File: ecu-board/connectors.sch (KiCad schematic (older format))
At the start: 34 parts, among them J10 Injector connector, J11 Cockpit connector, J12 EGO connector, J13 Chrankshaft Hall connector, J14 Camshaft Hall connector, J15 Ignition 1 connector, J16 Ignition 2 connector, J17 Camera connector, J18 Wheel Hall connector, J2 Battery power conenctor, J4 Motor connector, J5 Serial DB9 connector, J6 Controller connector, J7 Backlight connector, J8 IAT connector, J9 CLT connector

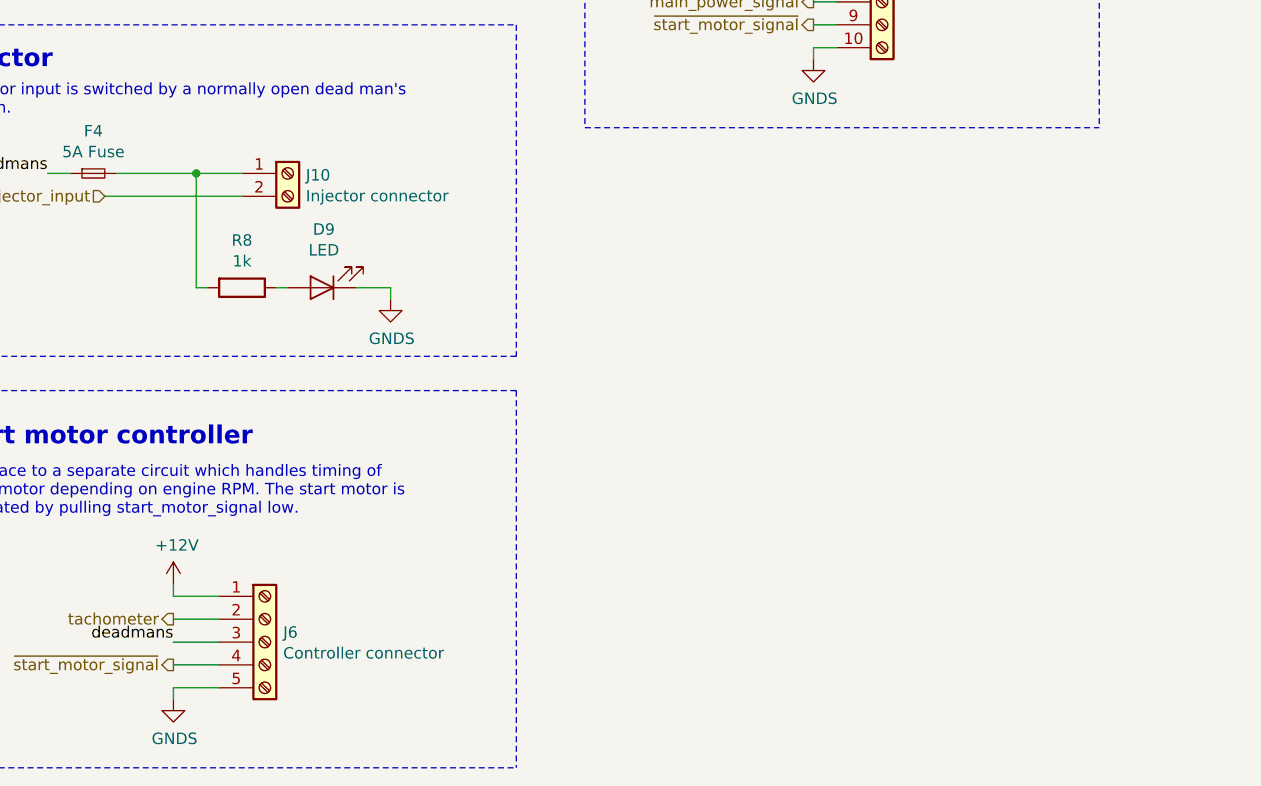
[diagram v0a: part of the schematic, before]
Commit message: Add CAN connector.
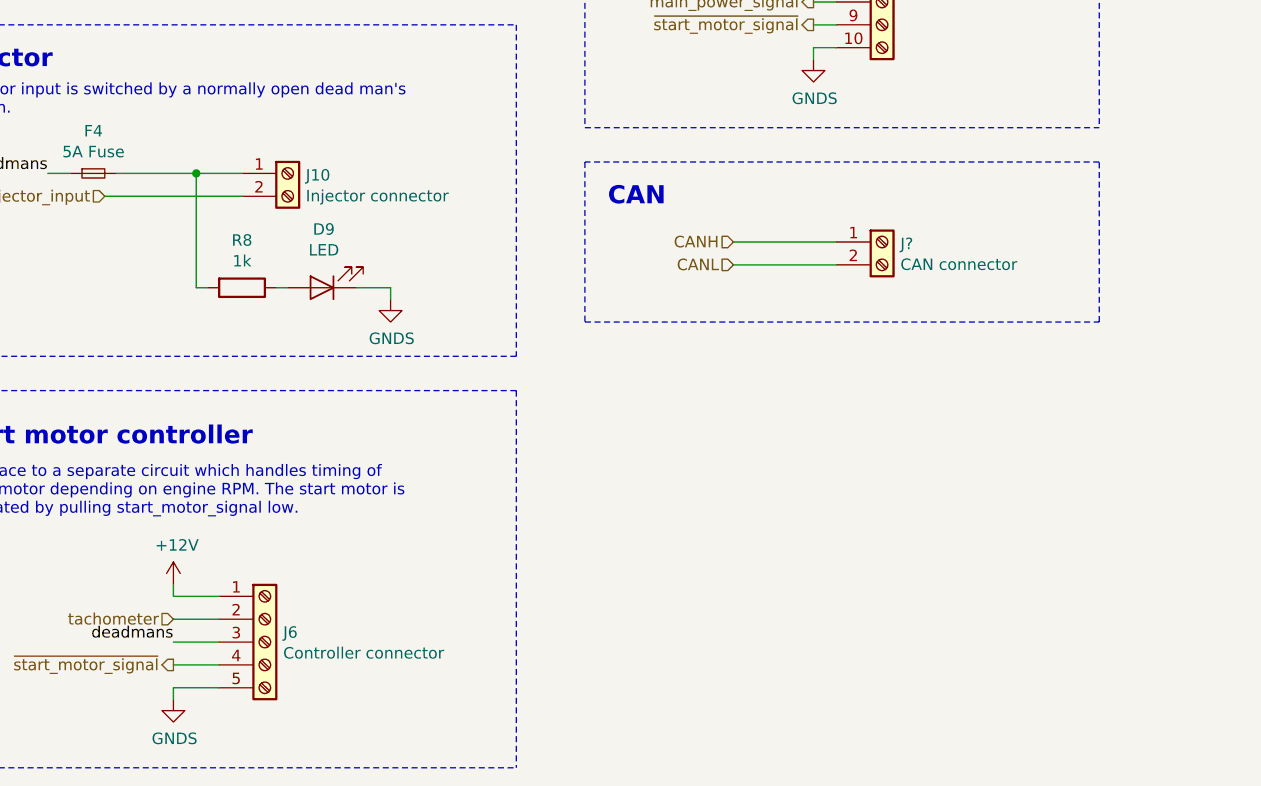
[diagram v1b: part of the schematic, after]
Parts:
- added J?: CAN connector, ecu-board-footprints:Terminal_Block_2x5.00mm, symbol Connector:Screw_Terminal_01x02
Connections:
- new net CANH: J?.1 (Pin_1)
- new net CANL: J?.2 (Pin_2)
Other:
- note added: "CAN"
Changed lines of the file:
@@
 	1    0    0    -1
 $EndComp
-Text HLabel 1900 9050 0    50   Output ~ 0
+Text HLabel 1900 9050 0    50   Input ~ 0
 tachometer
 Wire Wire Line
@@
 Wire Wire Line
 	1700 2300 2100 2300
+$Comp
+L Connector:Screw_Terminal_01x02 J?
+U 1 1 5D94B35C
+P 5000 7400
+F 0 "J?" H 5080 7392 50  0000 L CNN
+F 1 "CAN connector" H 5080 7301 50  0000 L CNN
+F 2 "ecu-board-footprints:Terminal_Block_2x5.00mm" H 5000 7400 50  0001 C CNN
+F 3 "~" H 5000 7400 50  0001 C CNN
+F 4 "Würth" H 5000 7400 50  0001 C CNN "Manufacturer"
+F 5 "2141 Series" H 5000 7400 50  0001 C CNN "Part no."
+	1    5000 7400
+	1    0    0    -1
+$EndComp
+Text Notes 3800 7250 0    79   ~ 16
+CAN
+Text HLabel 4350 7400 0    50   Input ~ 0
+CANH
+Text HLabel 4350 7500 0    50   Input ~ 0
+CANL
+Wire Wire Line
+	4350 7500 4800 7500
+Wire Wire Line
+	4800 7400 4350 7400
+Wire Notes Line
+	3700 7050 3700 7750
+Wire Notes Line
+	3700 7750 5950 7750
+Wire Notes Line
+	5950 7750 5950 7050
+Wire Notes Line
+	5950 7050 3700 7050
 $EndSCHEMATC

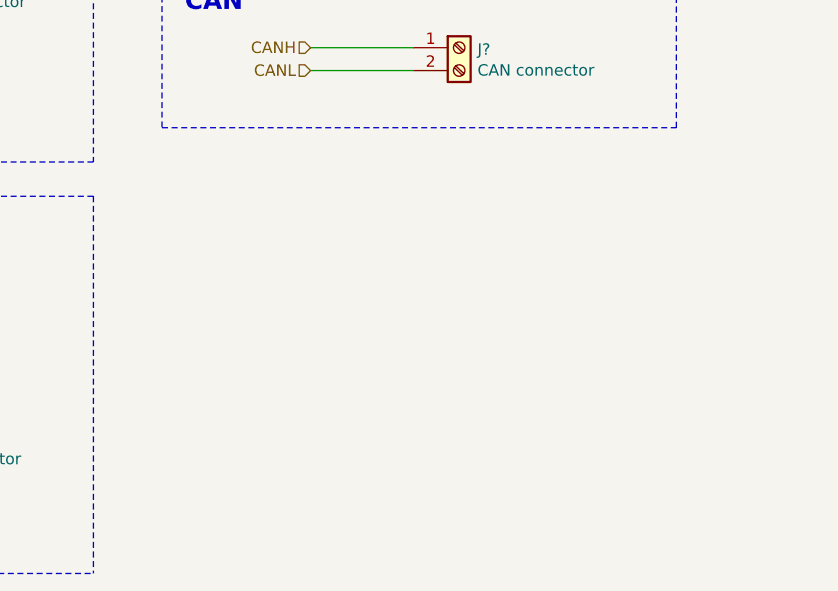
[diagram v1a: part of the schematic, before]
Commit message: Add speed sensor connector.
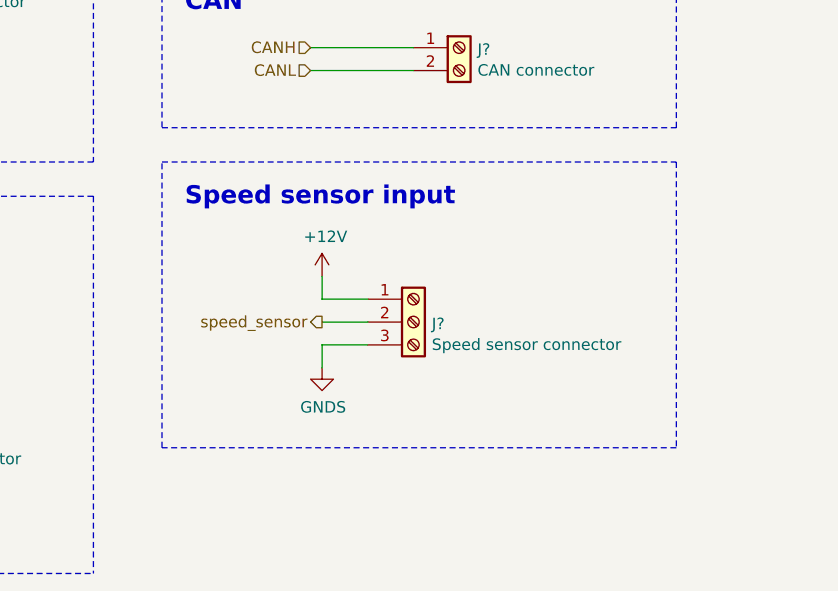
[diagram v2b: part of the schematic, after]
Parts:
- added J?: Speed sensor connector, ecu-board-footprints:Terminal_Block_3x5.00mm, symbol Connector:Screw_Terminal_01x03
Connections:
- net +12V: now also J?.1 (Pin_1)
- net GNDS: now also J?.3 (Pin_3)
- new net speed_sensor: J?.2 (Pin_2)
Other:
- note added: "Speed sensor input"
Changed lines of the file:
@@
 Wire Notes Line
 	5950 7050 3700 7050
+Text Notes 3800 8100 0    79   ~ 16
+Speed sensor input
+$Comp
+L Connector:Screw_Terminal_01x03 J?
+U 1 1 5DA598D9
+P 4800 8600
+F 0 "J?" H 4880 8592 50  0000 L CNN
+F 1 "Speed sensor connector" H 4880 8501 50  0000 L CNN
+F 2 "ecu-board-footprints:Terminal_Block_3x5.00mm" H 4800 8600 50  0001 C CNN
+F 3 "~" H 4800 8600 50  0001 C CNN
+F 4 "Würth" H 4800 8600 50  0001 C CNN "Manufacturer"
+F 5 "2141 Series" H 4800 8600 50  0001 C CNN "Part no."
+	1    4800 8600
+	1    0    0    -1
+$EndComp
+$Comp
+L power:GNDS #PWR?
+U 1 1 5DA6AA4C
+P 4400 8800
+F 0 "#PWR?" H 4400 8550 50  0001 C CNN
+F 1 "GNDS" H 4405 8627 50  0000 C CNN
+F 2 "" H 4400 8800 50  0001 C CNN
+F 3 "" H 4400 8800 50  0001 C CNN
+	1    4400 8800
+	1    0    0    -1
+$EndComp
+$Comp
+L power:+12V #PWR?
+U 1 1 5DA6B84B
+P 4400 8400
+F 0 "#PWR?" H 4400 8250 50  0001 C CNN
+F 1 "+12V" H 4415 8573 50  0000 C CNN
+F 2 "" H 4400 8400 50  0001 C CNN
+F 3 "" H 4400 8400 50  0001 C CNN
+	1    4400 8400
+	1    0    0    -1
+$EndComp
+Wire Wire Line
+	4400 8400 4400 8500
+Wire Wire Line
+	4400 8500 4600 8500
+Wire Wire Line
+	4600 8700 4400 8700
+Wire Wire Line
+	4400 8700 4400 8800
+Text HLabel 4400 8600 0    50   Output ~ 0
+speed_sensor
+Wire Wire Line
+	4400 8600 4600 8600
+Wire Notes Line
+	3700 7900 5950 7900
+Wire Notes Line
+	5950 7900 5950 9150
+Wire Notes Line
+	5950 9150 3700 9150
+Wire Notes Line
+	3700 9150 3700 7900
 $EndSCHEMATC

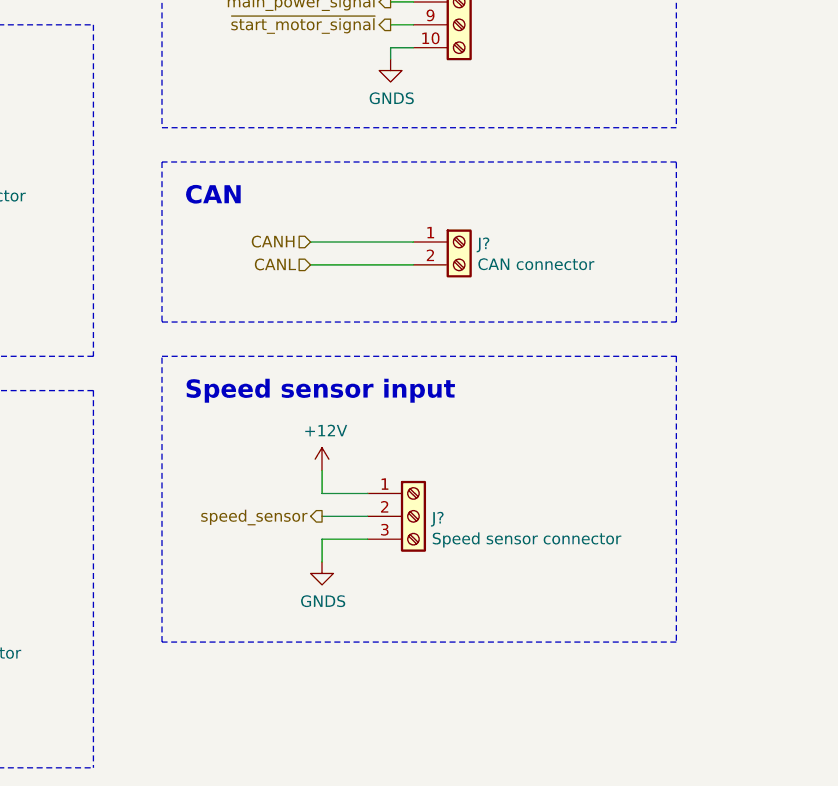
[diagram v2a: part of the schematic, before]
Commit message: Add CAN termination resitor.
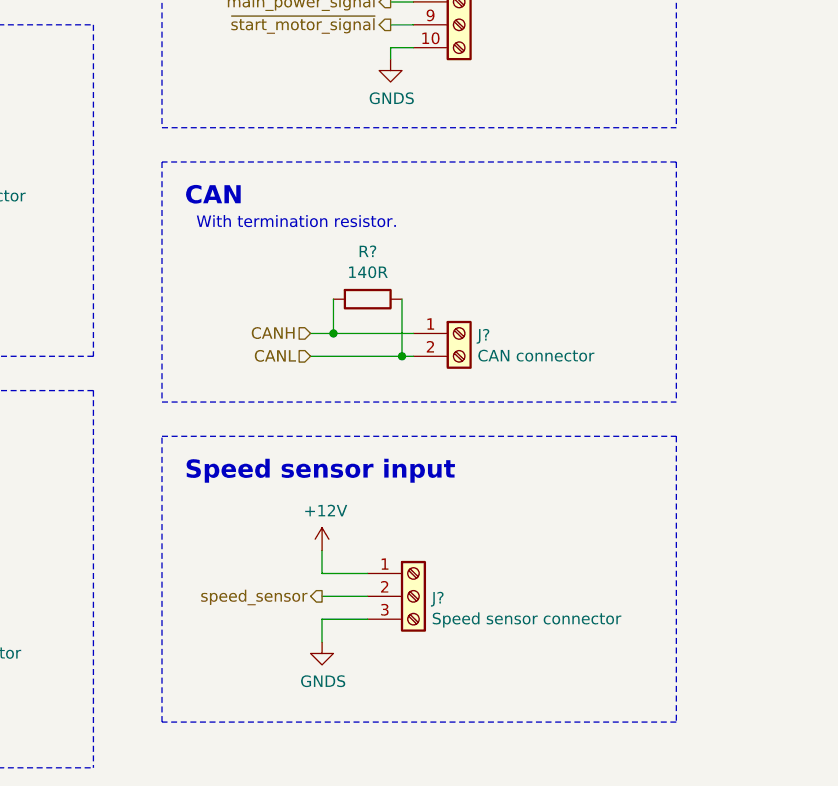
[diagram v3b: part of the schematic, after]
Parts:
- added R?: 140R, symbol Device:R
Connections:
- net CANH: now also R?.2
- net CANL: now also R?.1
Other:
- note added: "With termination resistor."
- moved on the sheet: J?
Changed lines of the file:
@@
 Wire Wire Line
 	1700 2300 2100 2300
-$Comp
-L Connector:Screw_Terminal_01x02 J?
-U 1 1 5D94B35C
-P 5000 7400
-F 0 "J?" H 5080 7392 50  0000 L CNN
-F 1 "CAN connector" H 5080 7301 50  0000 L CNN
-F 2 "ecu-board-footprints:Terminal_Block_2x5.00mm" H 5000 7400 50  0001 C CNN
-F 3 "~" H 5000 7400 50  0001 C CNN
-F 4 "Würth" H 5000 7400 50  0001 C CNN "Manufacturer"
-F 5 "2141 Series" H 5000 7400 50  0001 C CNN "Part no."
-	1    5000 7400
-	1    0    0    -1
-$EndComp
 Text Notes 3800 7250 0    79   ~ 16
 CAN
-Text HLabel 4350 7400 0    50   Input ~ 0
-CANH
-Text HLabel 4350 7500 0    50   Input ~ 0
-CANL
-Wire Wire Line
-	4350 7500 4800 7500
-Wire Wire Line
-	4800 7400 4350 7400
 Wire Notes Line
-	3700 7050 3700 7750
-Wire Notes Line
-	3700 7750 5950 7750
-Wire Notes Line
-	5950 7750 5950 7050
+	3700 8100 5950 8100
 Wire Notes Line
 	5950 7050 3700 7050
-Text Notes 3800 8100 0    79   ~ 16
+Text Notes 3800 8450 0    79   ~ 16
 Speed sensor input
 $Comp
 L Connector:Screw_Terminal_01x03 J?
 U 1 1 5DA598D9
-P 4800 8600
-F 0 "J?" H 4880 8592 50  0000 L CNN
-F 1 "Speed sensor connector" H 4880 8501 50  0000 L CNN
-F 2 "ecu-board-footprints:Terminal_Block_3x5.00mm" H 4800 8600 50  0001 C CNN
-F 3 "~" H 4800 8600 50  0001 C CNN
-F 4 "Würth" H 4800 8600 50  0001 C CNN "Manufacturer"
-F 5 "2141 Series" H 4800 8600 50  0001 C CNN "Part no."
-	1    4800 8600
+P 4800 8950
+F 0 "J?" H 4880 8942 50  0000 L CNN
+F 1 "Speed sensor connector" H 4880 8851 50  0000 L CNN
+F 2 "ecu-board-footprints:Terminal_Block_3x5.00mm" H 4800 8950 50  0001 C CNN
+F 3 "~" H 4800 8950 50  0001 C CNN
+F 4 "Würth" H 4800 8950 50  0001 C CNN "Manufacturer"
+F 5 "2141 Series" H 4800 8950 50  0001 C CNN "Part no."
+	1    4800 8950
 	1    0    0    -1
 $EndComp
@@
 L power:GNDS #PWR?
 U 1 1 5DA6AA4C
-P 4400 8800
-F 0 "#PWR?" H 4400 8550 50  0001 C CNN
-F 1 "GNDS" H 4405 8627 50  0000 C CNN
-F 2 "" H 4400 8800 50  0001 C CNN
-F 3 "" H 4400 8800 50  0001 C CNN
-	1    4400 8800
+P 4400 9150
+F 0 "#PWR?" H 4400 8900 50  0001 C CNN
+F 1 "GNDS" H 4405 8977 50  0000 C CNN
+F 2 "" H 4400 9150 50  0001 C CNN
+F 3 "" H 4400 9150 50  0001 C CNN
+	1    4400 9150
 	1    0    0    -1
 $EndComp
@@
 L power:+12V #PWR?
 U 1 1 5DA6B84B
-P 4400 8400
-F 0 "#PWR?" H 4400 8250 50  0001 C CNN
-F 1 "+12V" H 4415 8573 50  0000 C CNN
-F 2 "" H 4400 8400 50  0001 C CNN
-F 3 "" H 4400 8400 50  0001 C CNN
-	1    4400 8400
+P 4400 8750
+F 0 "#PWR?" H 4400 8600 50  0001 C CNN
+F 1 "+12V" H 4415 8923 50  0000 C CNN
+F 2 "" H 4400 8750 50  0001 C CNN
+F 3 "" H 4400 8750 50  0001 C CNN
+	1    4400 8750
 	1    0    0    -1
 $EndComp
 Wire Wire Line
-	4400 8400 4400 8500
+	4400 8750 4400 8850
 Wire Wire Line
-	4400 8500 4600 8500
+	4400 8850 4600 8850
 Wire Wire Line
-	4600 8700 4400 8700
+	4600 9050 4400 9050
 Wire Wire Line
-	4400 8700 4400 8800
-Text HLabel 4400 8600 0    50   Output ~ 0
+	4400 9050 4400 9150
+Text HLabel 4400 8950 0    50   Output ~ 0
 speed_sensor
 Wire Wire Line
-	4400 8600 4600 8600
+	4400 8950 4600 8950
 Wire Notes Line
-	3700 7900 5950 7900
+	3700 8250 5950 8250
 Wire Notes Line
-	5950 7900 5950 9150
+	5950 8250 5950 9500
 Wire Notes Line
-	5950 9150 3700 9150
+	5950 9500 3700 9500
 Wire Notes Line
-	3700 9150 3700 7900
+	3700 9500 3700 8250
+Text Notes 3850 7350 0    50   ~ 0
+With termination resistor.
+Wire Notes Line
+	3700 7050 3700 8100
+Wire Notes Line
+	5950 7050 5950 8100
+Wire Wire Line
+	4750 7900 4800 7900
+Connection ~ 4750 7900
+Wire Wire Line
+	4750 7650 4750 7900
+Wire Wire Line
+	4450 7800 4350 7800
+Connection ~ 4450 7800
+Wire Wire Line
+	4450 7650 4450 7800
+$Comp
+L Device:R R?
+U 1 1 5DAC1E2A
+P 4600 7650
+F 0 "R?" V 4393 7650 50  0000 C CNN
+F 1 "140R" V 4484 7650 50  0000 C CNN
+F 2 "" V 4530 7650 50  0001 C CNN
+F 3 "~" H 4600 7650 50  0001 C CNN
+	1    4600 7650
+	0    1    1    0
+$EndComp
+Wire Wire Line
+	4800 7800 4450 7800
+Wire Wire Line
+	4350 7900 4750 7900
+Text HLabel 4350 7900 0    50   Input ~ 0
+CANL
+Text HLabel 4350 7800 0    50   Input ~ 0
+CANH
+$Comp
+L Connector:Screw_Terminal_01x02 J?
+U 1 1 5D94B35C
+P 5000 7800
+F 0 "J?" H 5080 7792 50  0000 L CNN
+F 1 "CAN connector" H 5080 7701 50  0000 L CNN
+F 2 "ecu-board-footprints:Terminal_Block_2x5.00mm" H 5000 7800 50  0001 C CNN
+F 3 "~" H 5000 7800 50  0001 C CNN
+F 4 "Würth" H 5000 7800 50  0001 C CNN "Manufacturer"
+F 5 "2141 Series" H 5000 7800 50  0001 C CNN "Part no."
+	1    5000 7800
+	1    0    0    -1
+$EndComp
 $EndSCHEMATC
